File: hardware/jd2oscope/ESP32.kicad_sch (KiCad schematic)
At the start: 1 part, among them U2 ESP32-S3-WROOM-2

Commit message: feat: kicad board dev
parts added, general framework established
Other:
- note removed: "Onboard ADC is good enough so long as you disable the onboard wifi"
- moved on the sheet: U2
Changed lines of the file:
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@@
 	(generator_version "8.0")
 	(paper "A4")
-	(rectangle
-		(start 132.08 50.8)
-		(end 204.47 57.15)
-		(stroke
-			(width 0)
-			(type default)
-		)
-		(fill
-			(type none)
-		)
-	)
-	(text "Onboard ADC is good enough so long as you disable the onboard wifi"
-		(exclude_from_sim no)
-		(at 168.148 54.356 0)
-		(effects
-			(font
-				(size 1.27 1.27)
-			)
-		)
-	)
 	(symbol
 		(lib_id "RF_Module:ESP32-S3-WROOM-2")
-		(at 92.71 67.31 0)
+		(at 92.71 83.82 0)
 		(unit 1)
 		(exclude_from_sim no)
@@
 		(fields_autoplaced yes)
 		(property "Reference" "U2"
-			(at 94.9041 16.51 0)
+			(at 94.9041 33.02 0)
 			(effects
 				(font
@@
 		)
 		(property "Value" "ESP32-S3-WROOM-2"
-			(at 94.9041 19.05 0)
+			(at 94.9041 35.56 0)
 			(effects
 				(font
@@
 		)
 		(property "Footprint" "RF_Module:ESP32-S3-WROOM-2"
-			(at 92.71 128.27 0)
+			(at 92.71 144.78 0)
 			(effects
 				(font
@@
 		)
 		(property "Datasheet" "https://www.espressif.com/sites/default/files/documentation/esp32-s3-wroom-2_datasheet_en.pdf"
-			(at 92.71 130.81 0)
+			(at 92.71 147.32 0)
 			(effects
 				(font
@@
 		)
 		(property "Description" "RF Module, 2.4 GHz, Wi­-Fi, Bluetooth, BLE, ESP32­-S3R8V"
-			(at 92.71 67.31 0)
+			(at 92.71 83.82 0)
 			(effects
 				(font

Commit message: fix: pushing so people can edit!! (I think)
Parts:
- removed U2: ESP32-S3-WROOM-2, RF_Module:ESP32-S3-WROOM-2, symbol RF_Module:ESP32-S3-WROOM-2
- added U5: ESP32-DEVKITC-32D, digikey-footprints:MODULE_ESP32-DEVKITC-32D, symbol ESP32-DEVKITC-32D:ESP32-DEVKITC-32D
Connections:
- new net 3.3V: U5.J2-1 (3V3)
- new net 5V: U5.J2-19 (EXT_5V)
- new net GND: U5.J2-14 (GND1), U5.J3-1 (GND3), U5.J3-7 (GND2)

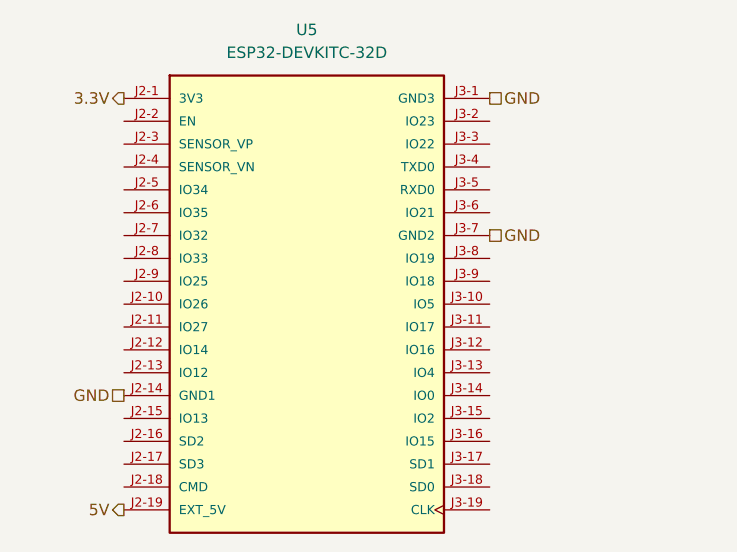
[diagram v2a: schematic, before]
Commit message: feat: screen implemented
alongside screen implementation, re-structured layout for schematics, and cleaned up SPI comm. conn.s; also implemented ADC module successfully (sans SPI section for it; that comes next)
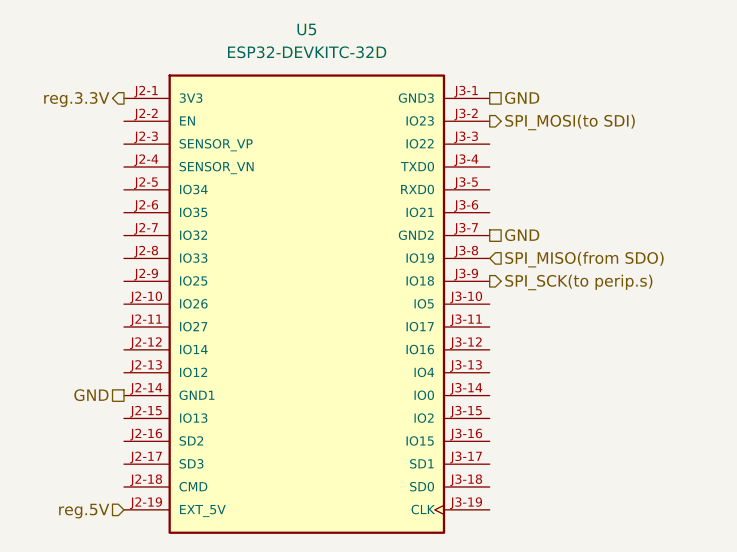
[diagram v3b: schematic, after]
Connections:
- net SPI_MOSI(to SDI): now reaches U5.J3-2 (IO23)
- net SPI_MISO(from SDO): now reaches U5.J3-8 (IO19)
- net SPI_SCK(to perip.s): now reaches U5.J3-9 (IO18)
- net 3.3V renamed reg.3.3V
- net 5V renamed reg.5V
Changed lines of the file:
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@@
 		(shape passive)
 		(at 154.94 48.26 0)
+		(fields_autoplaced yes)
+		(effects
+			(font
+				(size 1.27 1.27)
+			)
+			(justify left)
+		)
+	)
+	(hierarchical_label "SPI_SCK(to perip.s)"
+		(shape output)
+		(at 154.94 68.58 0)
+		(fields_autoplaced yes)
+		(effects
+			(font
+				(size 1.27 1.27)
+			)
+			(justify left)
+		)
+	)
+	(hierarchical_label "SPI_MOSI(to SDI)"
+		(shape output)
+		(at 154.94 50.8 0)
+		(fields_autoplaced yes)
 		(effects
 			(font
@@
 		(shape passive)
 		(at 114.3 81.28 180)
+		(fields_autoplaced yes)
 		(effects
 			(font
@@
 		)
 	)
-	(hierarchical_label "3.3V"
+	(hierarchical_label "SPI_MISO(from SDO)"
+		(shape input)
+		(at 154.94 66.04 0)
+		(fields_autoplaced yes)
+		(effects
+			(font
+				(size 1.27 1.27)
+			)
+			(justify left)
+		)
+	)
+	(hierarchical_label "reg.3.3V"
 		(shape output)
 		(at 114.3 48.26 180)
+		(fields_autoplaced yes)
 		(effects
 			(font
@@
 		)
 	)
-	(hierarchical_label "5V"
-		(shape output)
+	(hierarchical_label "reg.5V"
+		(shape input)
 		(at 114.3 93.98 180)
+		(fields_autoplaced yes)
 		(effects
 			(font
@@
 		(shape passive)
 		(at 154.94 63.5 0)
+		(fields_autoplaced yes)
 		(effects
 			(font
@@
 				(hide yes)
 			)
+		)
+		(property "Sim.Device" ""
+			(at 134.62 71.12 0)
+			(effects
+				(font
+					(size 1.27 1.27)
+				)
+				(hide yes)
+			)
+		)
+		(property "Sim.Params" ""
+			(at 134.62 71.12 0)
+			(effects
+				(font
+					(size 1.27 1.27)
+				)
+				(hide yes)
+			)
+		)
+		(property "Sim.Pins" ""
+			(at 134.62 71.12 0)
+			(effects
+				(font
+					(size 1.27 1.27)
+				)
+				(hide yes)
+			)
+		)
+		(property "Sim.Type" ""
+			(at 134.62 71.12 0)
+			(effects
+				(font
+					(size 1.27 1.27)
+				)
+				(hide yes)
+			)
